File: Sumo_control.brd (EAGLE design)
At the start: 60 x 22.5 mm, 14 parts, among them X1 MICROMATCH-8

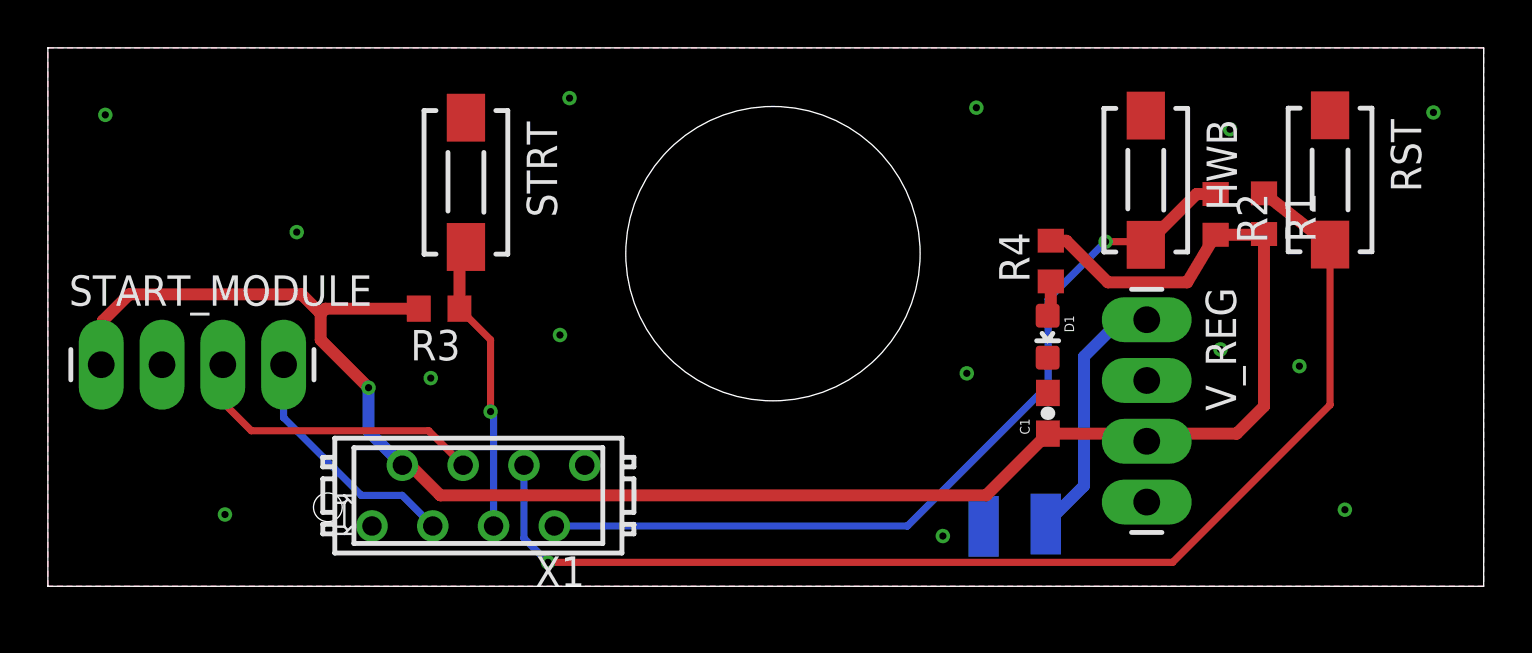
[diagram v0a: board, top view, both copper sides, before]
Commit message: Replace power pads with bigger ones
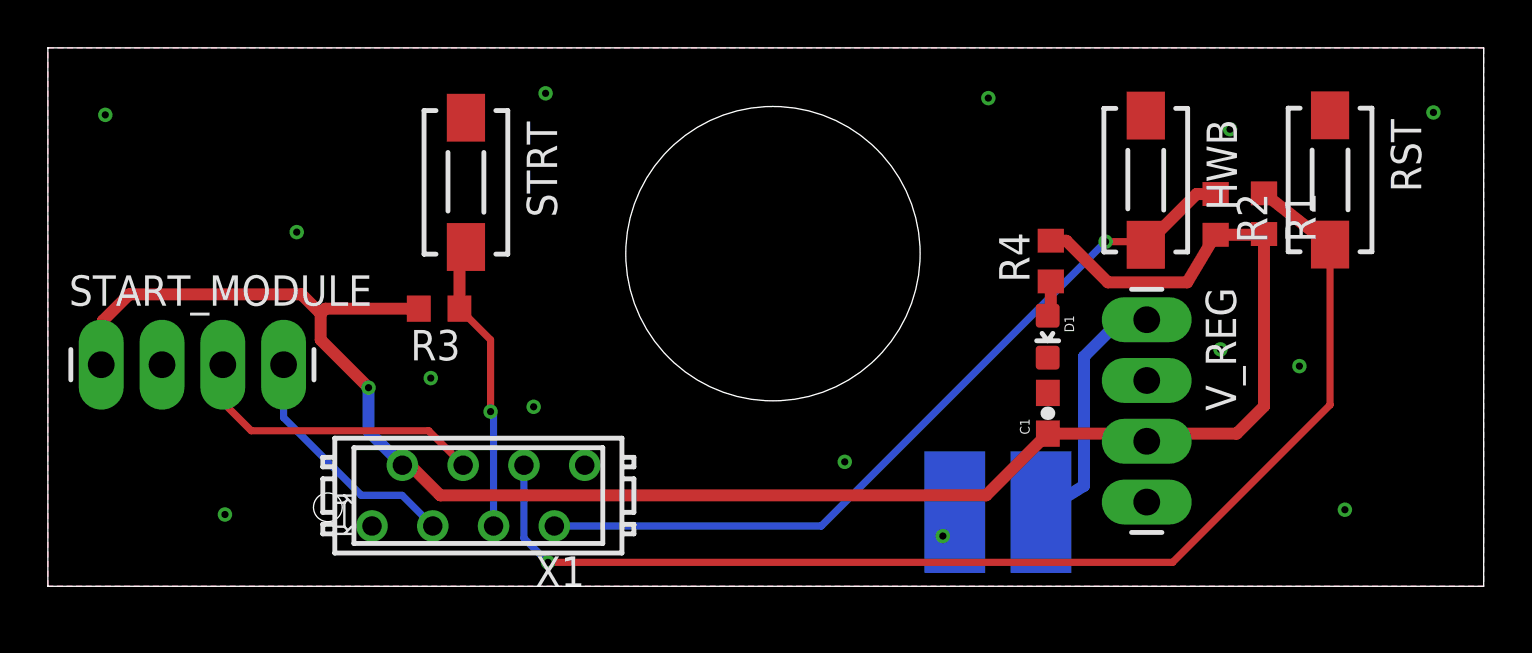
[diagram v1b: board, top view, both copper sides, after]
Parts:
- GND_PAD, V_PAD: value (none) -> WIREPADSMD2,54-5,08; device wirepad:SMD1,27-2,54 -> wirepad:SMD2,54-5,08
- moved GND_PAD 1.34 mm to (37.9, 3.10)
- moved V_PAD 0.54 mm to (41.5, 3.10)
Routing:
- net HWB: track 35.6 -> 33.5 mm
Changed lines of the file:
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@@
 <element name="D1" library="SparkFun-LED" package="LED-0603" value="PWR_LED" x="41.78" y="10.43" rot="R180"/>
 <element name="R4" library="resistor" package="R0603" value="1k" x="41.91" y="13.59" rot="R90"/>
-<element name="GND_PAD" library="wirepad" package="SMD1,27-2,54" value="" x="39.1" y="2.5" rot="MR0"/>
-<element name="V_PAD" library="wirepad" package="SMD1,27-2,54" value="" x="41.7" y="2.6" rot="MR0"/>
+<element name="GND_PAD" library="wirepad" package="SMD2,54-5,08" value="WIREPADSMD2,54-5,08" x="37.9" y="3.1" rot="MR0"/>
+<element name="V_PAD" library="wirepad" package="SMD2,54-5,08" value="WIREPADSMD2,54-5,08" x="41.5" y="3.1" rot="MR0"/>
 </elements>
 <signals>
@@
 <via x="52.3" y="9.2" extent="1-16" drill="0.3"/>
 <via x="54.2" y="3.2" extent="1-16" drill="0.3"/>
-<via x="21.4" y="10.5" extent="1-16" drill="0.3"/>
+<via x="20.3" y="7.5" extent="1-16" drill="0.3"/>
 <via x="2.4" y="19.7" extent="1-16" drill="0.3"/>
-<via x="21.8" y="20.4" extent="1-16" drill="0.3"/>
-<via x="38.8" y="20" extent="1-16" drill="0.3"/>
-<via x="38.4" y="8.9" extent="1-16" drill="0.3"/>
+<via x="20.8" y="20.6" extent="1-16" drill="0.3"/>
+<via x="39.3" y="20.4" extent="1-16" drill="0.3"/>
+<via x="33.3" y="5.2" extent="1-16" drill="0.3"/>
 <via x="57.9" y="19.8" extent="1-16" drill="0.3"/>
 <via x="37.4" y="2.1" extent="1-16" drill="0.3"/>
@@
 <contactref element="HWB" pad="2"/>
 <contactref element="X1" pad="7"/>
-<wire x1="21.165" y1="2.52" x2="35.92" y2="2.52" width="0.3" layer="16"/>
-<wire x1="35.92" y1="2.52" x2="41.8" y2="8.4" width="0.3" layer="16"/>
-<wire x1="41.8" y1="8.4" x2="41.8" y2="12" width="0.3" layer="16"/>
-<wire x1="41.8" y1="12" x2="44.2" y2="14.4" width="0.3" layer="16"/>
 <via x="44.2" y="14.4" extent="1-16" drill="0.3"/>
 <wire x1="44.2" y1="14.4" x2="45.75" y2="14.4" width="0.3" layer="1"/>
@@
 <wire x1="48.8" y1="16.39" x2="48" y2="16.39" width="0.5" layer="1"/>
 <wire x1="48" y1="16.39" x2="45.88" y2="14.27" width="0.5" layer="1"/>
+<wire x1="44.2" y1="14.4" x2="32.32" y2="2.52" width="0.3" layer="16"/>
+<wire x1="32.32" y1="2.52" x2="21.165" y2="2.52" width="0.3" layer="16"/>
 </signal>
 <signal name="START_BTN">
@@
 <contactref element="V_REG" pad="1"/>
 <contactref element="V_PAD" pad="1"/>
-<wire x1="41.7" y1="2.6" x2="43.3" y2="4.2" width="0.5" layer="16"/>
+<wire x1="41.5" y1="3.1" x2="43.3" y2="4.2" width="0.5" layer="16"/>
 <wire x1="43.3" y1="4.2" x2="43.3" y2="9.6" width="0.5" layer="16"/>
 <wire x1="43.3" y1="9.6" x2="44.84" y2="11.14" width="0.5" layer="16"/>

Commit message: Final modifications before test order
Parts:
- moved R4 2.11 mm to (40.8, 11.8)
- moved R2 2.01 mm to (48.6, 13.5)
- moved R1 2.00 mm to (50.7, 13.6)
- moved D1 1.67 mm to (42.6, 11.9), turned to 0 degrees
- moved R3 0.40 mm to (16.4, 12.0)
- moved HWB 0.20 mm to (45.7, 17.0)
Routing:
- net VCC: track 80.2 -> 76.9 mm, vias 1 -> 0
- net GND: track 0.00 -> 1.11 mm, vias 14 -> 9
- net START: track 12.7 -> 13.7 mm
- net RESET: track 50.5 -> 49.5 mm
- net HWB: track 33.5 -> 32.8 mm
- net N$1: track 1.49 -> 2.01 mm
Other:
- board text added: "+"
- board text added: "HWB"
- board text added: "RESET"
- board text added: "START"
